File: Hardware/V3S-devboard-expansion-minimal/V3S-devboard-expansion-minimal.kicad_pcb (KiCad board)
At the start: 2 copper layers, 67.3 x 87.1 mm, 48 parts, among them CN1 AS0BC21-S30BE-7H, J1 Conn_01x05_Pin, J10 USB_C_Receptacle_USB2.0, J11 Conn_01x02_Pin, J12 Conn_02x05_Odd_Even, J13 Conn_01x03_Pin, J16 Conn_01x04_MountingPin, J17 Conn_01x04_MountingPin, J2 Conn_01x05_Pin, J3 Conn_01x05_Pin, J4 Conn_01x02_Pin, J5 Conn_02x05_Odd_Even, J6 Conn_01x02_Pin, J7 Conn_02x12_Odd_Even, J8 RJ45_Hanrun_HR911105A_Horizon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, U1 CP2102N-Axx-xQFN28, U3 AMS1117-3.3, U4 AMS1117-2.85

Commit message: working on final touches
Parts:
- added H1: MountingHole_Pad, v3s-devboard-expansion-minimal:screwnut, F.Cu at (98.5, 82.3)
- added R15: 8.2K, Resistor_SMD:R_0603_1608Metric, F.Cu at (81.0, 75.6)
- added R16: 10K, Resistor_SMD:R_0603_1608Metric, F.Cu at (81.0, 80.3)
- added R17: 11K, Resistor_SMD:R_0603_1608Metric, F.Cu at (81.0, 85.0)
- added R18: 6.8K, Resistor_SMD:R_0603_1608Metric, F.Cu at (81.7, 72.1)
- added SW1: SW_MEC_5E, v3s-devboard-module:SW_SKRPACE010, F.Cu at (75.6, 152.4)
- added SW2: SW_MEC_5E, v3s-devboard-module:SW_SKRPACE010, F.Cu at (77.0, 73.1)
- added SW3: SW_MEC_5E, v3s-devboard-module:SW_SKRPACE010, F.Cu at (77.0, 77.8)
- added SW4: SW_MEC_5E, v3s-devboard-module:SW_SKRPACE010, F.Cu at (77.0, 82.6)
- added SW5: SW_MEC_5E, v3s-devboard-module:SW_SKRPACE010, F.Cu at (77.0, 87.3)
- C5, C6: moved to B.Cu
- J16, J17: moved to F.Cu
- moved R6 114.0 mm to (74.8, 148.6)
- moved C6 23.6 mm to (134.7, 144.1)
- moved C5 21.9 mm to (134.7, 142.5)
- moved J17 21.8 mm to (134.1, 123.7), turned to 90 degrees
- moved JP8 19.7 mm to (125.6, 125.3)
- moved JP6 19.7 mm to (128.5, 122.2)
- moved J10 12.1 mm to (131.1, 153.0), turned to 0 degrees
- moved JP5 11.2 mm to (129.2, 108.9)
- moved JP7 11.2 mm to (126.3, 111.5)
- moved R14 10.0 mm to (133.7, 146.5), turned to 0 degrees
- moved J12 9.94 mm to (121.5, 116.4), turned to 0 degrees
- moved J16 9.57 mm to (134.1, 108.0), turned to 90 degrees
- moved R13 8.38 mm to (136.8, 138.5)
- moved U1 8.38 mm to (131.7, 138.3)
- moved C3 7.47 mm to (136.8, 141.7)
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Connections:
- J13 pad 2: LED_VDD -> LCD_VDD
- J3 pad 1: LED_VDD -> LCD_VDD
- J3 pad 2: LED_VDD -> LCD_VDD
- J3 pad 3: LED_VDD -> LCD_VDD
- J3 pad 4: LED_VDD -> LCD_VDD
- J3 pad 5: LED_VDD -> LCD_VDD
- J4 pad 1: LED_VDD -> LCD_VDD
- J7 pad 19: 3V3 -> GND
- J7 pad 20: GND -> 3V3
- J7 pad 21: 3V3 -> GND
- J7 pad 22: GND -> 3V3
- J7 pad 23: 3V3 -> GND
- J7 pad 24: GND -> 3V3
- R6 pad 1: LED_VDD -> LCD_VDD
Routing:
- net 3V3: track 99.0 -> 179.3 mm, vias 1 -> 5
- net /LRADC0: track 0.00 -> 73.8 mm, vias 0 -> 4
- net LCD_VDD: track 0.00 -> 73.4 mm, vias 0 -> 1
- net /SDC1.CLK: track 0.00 -> 63.6 mm, vias 0 -> 4
- net /SDC1.D0: track 0.00 -> 59.2 mm, vias 0 -> 4
- net /RESET: track 0.00 -> 51.3 mm, vias 0 -> 2
- net /USB.USB_ID: track 0.00 -> 44.5 mm, vias 0 -> 2
- net /LEDA: track 0.00 -> 36.4 mm
- net /CSI.MCSI_D0_N: track 24.2 -> 47.6 mm, vias 1 -> 2
- net /CSI.MCSI_D1_P: track 23.8 -> 46.2 mm, vias 1 -> 2
- net /CSI.MCSI_D1_N: track 23.2 -> 42.9 mm, vias 1 -> 2
- net /UART0.RX: track 40.1 -> 59.5 mm
- net /VBUS_IN: track 66.6 -> 86.0 mm
- net Net-(J12-Pin_1): track 28.5 -> 45.6 mm
- net /UART2.RX: track 57.9 -> 45.4 mm, vias 2 -> 3
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- added copper zone on B.Cu, net GND
- added copper zone on F.Cu, net GND
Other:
- board size 67.3 x 87.1 mm -> 68.5 x 88 mm

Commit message: Minor changes. Sent to fab
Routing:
- net /LCD_TE: track 48.4 -> 51.2 mm
- net /CSI.CSI_SDA: track 32.0 -> 34.7 mm
- net /UART0.TX: vias 6 -> 5
- net /UART0.RX: vias 4 -> 3
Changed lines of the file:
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@@
 		(sheetname "Root")
 		(sheetfile "V3S-devboard-expansion-minimal.kicad_sch")
-		(attr through_hole)
+		(attr through_hole exclude_from_bom)
 		(fp_line
 			(start 1.33 -1.33)
@@
 		(sheetname "Root")
 		(sheetfile "V3S-devboard-expansion-minimal.kicad_sch")
-		(attr smd)
+		(attr smd exclude_from_bom)
 		(fp_line
 			(start -4.04 -5.84)
@@
 			)
 		)
-		(property "LCSC" "C60491"
+		(property "LCSC" "C23212"
 			(at 0 0 180)
 			(unlocked yes)
@@
 		(sheetname "Root")
 		(sheetfile "V3S-devboard-expansion-minimal.kicad_sch")
-		(attr smd)
+		(attr smd exclude_from_bom)
 		(fp_line
 			(start -0.237258 0.5225)
@@
 		(sheetname "Root")
 		(sheetfile "V3S-devboard-expansion-minimal.kicad_sch")
-		(attr through_hole)
+		(attr through_hole exclude_from_bom)
 		(fp_line
 			(start -1.33 -1.33)
@@
 		(sheetname "Root")
 		(sheetfile "V3S-devboard-expansion-minimal.kicad_sch")
-		(attr smd)
+		(attr smd exclude_from_bom)
 		(fp_line
 			(start -0.237258 0.5225)
@@
 		(sheetname "Root")
 		(sheetfile "V3S-devboard-expansion-minimal.kicad_sch")
-		(attr through_hole)
+		(attr through_hole exclude_from_bom)
 		(fp_line
 			(start -1.33 -1.33)
@@
 			)
 		)
+		(property "LCSC" "C2928188"
+			(at 0 0 0)
+			(unlocked yes)
+			(layer "F.Fab")
+			(hide yes)
+			(effects
+				(font
+					(size 1 1)
+					(thickness 0.15)
+				)
+			)
+		)
 		(property ki_fp_filters "MountingHole*Pad*")
 		(sheetname "Root")
@@
 		(sheetname "Root")
 		(sheetfile "V3S-devboard-expansion-minimal.kicad_sch")
-		(attr through_hole)
+		(attr through_hole exclude_from_bom)
 		(fp_line
 			(start 3.87 -1.33)
@@
 		(sheetname "Root")
 		(sheetfile "V3S-devboard-expansion-minimal.kicad_sch")
-		(attr smd)
+		(attr smd exclude_from_bom)
 		(fp_line
 			(start -0.237258 0.5225)
@@
 		(sheetname "Root")
 		(sheetfile "V3S-devboard-expansion-minimal.kicad_sch")
-		(attr through_hole)
+		(attr through_hole exclude_from_bom)
 		(fp_line
 			(start -1.33 3.87)
@@
 			)
 		)
-		(property "LCSC" "C60491"
+		(property "LCSC" "C103227"
 			(at 0 0 -90)
 			(unlocked yes)
@@
 			)
 		)
+		(property "LCSC" "C139797"
+			(at 0 0 180)
+			(unlocked yes)
+			(layer "F.Fab")
+			(hide yes)
+			(effects
+				(font
+					(size 1 1)
+					(thickness 0.15)
+				)
+			)
+		)
 		(property ki_fp_filters "SW*MEC*5G*")
 		(sheetname "Root")
@@
 			)
 		)
+		(property "LCSC" "C139797"
+			(at 0 0 90)
+			(unlocked yes)
+			(layer "F.Fab")
+			(hide yes)
+			(effects
+				(font
+					(size 1 1)
+					(thickness 0.15)
+				)
+			)
+		)
 		(property ki_fp_filters "SW*MEC*5G*")
 		(sheetname "Root")
@@
 			)
 		)
+		(property "LCSC" "C2685134"
+			(at 0 0 180)
+			(unlocked yes)
+			(layer "F.Fab")
+			(hide yes)
+			(effects
+				(font
+					(size 1 1)
+					(thickness 0.15)
+				)
+			)
+		)
 		(property ki_fp_filters "Connector*:*_2x??_*")
 		(sheetname "Root")
@@
 			)
 		)
-		(property "LCSC" "C60491"
+		(property "LCSC" "C25804"
 			(at 0 0 -90)
 			(unlocked yes)
@@
 		(sheetname "Root")
 		(sheetfile "V3S-devboard-expansion-minimal.kicad_sch")
-		(attr smd)
+		(attr smd exclude_from_bom)
 		(fp_line
 			(start -0.237258 0.5225)
@@
 			)
 		)
+		(property "LCSC" "C2894897"
+			(at 0 0 0)
+			(unlocked yes)
+			(layer "F.Fab")
+			(hide yes)
+			(effects
+				(font
+					(size 1 1)
+					(thickness 0.15)
+				)
+			)
+		)
 		(property ki_fp_filters "USB*C*Receptacle*")
 		(sheetname "Root")
@@
 			)
 		)
-		(property "LCSC" "C60491"
+		(property "LCSC" "C25981"
 			(at 0 0 -90)
 			(unlocked yes)
@@
 		(sheetname "Root")
 		(sheetfile "V3S-devboard-expansion-minimal.kicad_sch")
-		(attr through_hole)
+		(attr through_hole exclude_from_bom)
 		(fp_line
 			(start -1.33 -1.33)
@@
 			)
 		)
+		(property "LCSC" "C139797"
+			(at 0 0 180)
+			(unlocked yes)
+			(layer "F.Fab")
+			(hide yes)
+			(effects
+				(font
+					(size 1 1)
+					(thickness 0.15)
+				)
+			)
+		)
 		(property ki_fp_filters "SW*MEC*5G*")
 		(sheetname "Root")
@@
 		(sheetname "Root")
 		(sheetfile "V3S-devboard-expansion-minimal.kicad_sch")
-		(attr through_hole)
+		(attr through_hole exclude_from_bom)
 		(fp_line
 			(start -1.33 -1.33)
@@
 		(sheetname "Root")
 		(sheetfile "V3S-devboard-expansion-minimal.kicad_sch")
-		(attr through_hole)
+		(attr through_hole exclude_from_bom)
 		(fp_line
 			(start -1.33 -1.33)
@@
 			)
 		)
+		(property "LCSC" "C139797"
+			(at 0 0 180)
+			(unlocked yes)
+			(layer "F.Fab")
+			(hide yes)
+			(effects
+				(font
+					(size 1 1)
+					(thickness 0.15)
+				)
+			)
+		)
 		(property ki_fp_filters "SW*MEC*5G*")
 		(sheetname "Root")
@@
 		(sheetname "Root")
 		(sheetfile "V3S-devboard-expansion-minimal.kicad_sch")
-		(attr smd)
+		(attr smd exclude_from_bom)
 		(fp_line
 			(start -0.153641 -0.38)
@@
 			)
 		)
+		(property "LCSC" "C139797"
+			(at 0 0 180)
+			(unlocked yes)
+			(layer "F.Fab")
+			(hide yes)
+			(effects
+				(font
+					(size 1 1)
+					(thickness 0.15)
+				)
+			)
+		)
 		(property ki_fp_filters "SW*MEC*5G*")
 		(sheetname "Root")
@@
 		(sheetname "Root")
 		(sheetfile "V3S-devboard-expansion-minimal.kicad_sch")
-		(attr smd)
+		(attr smd exclude_from_bom)
 		(fp_line
 			(start 0.140581 0.51)
@@
 		(sheetname "Root")
 		(sheetfile "V3S-devboard-expansion-minimal.kicad_sch")
-		(attr smd)
+		(attr smd exclude_from_bom)
 		(fp_line
 			(start 0.140581 0.51)
@@
 		(net 5)
 	)
-	(via
-		(at 129.24 107.555001)
-		(size 0.25)
-		(drill 0.15)
-		(layers "F.Cu" "B.Cu")
-		(net 5)
-	)
 	(segment
 		(start 107.215 136.355)
@@
 		(net 37)
 	)
-	(via
-		(at 129.34 110.155001)
-		(size 0.25)
-		(drill 0.15)
-		(layers "F.Cu" "B.Cu")
-		(net 37)
-	)
 	(segment
 		(start 114.93 127.27)
@@
 	)
 	(segment
+		(start 86.84 117.5)
+		(end 86.84 117.47)
+		(width 0.127)
+		(layer "F.Cu")
+		(net 55)
+	)
+	(segment
+		(start 86.84 117.47)
+		(end 80.885 111.515)
+		(width 0.127)
+		(layer "F.Cu")
+		(net 55)
+	)
+	(segment
 		(start 88.59 123.61)
 		(end 96.04 131.06)
@@
 	)
 	(segment
-		(start 87.59 122.54)
-		(end 87.59 122.59)
-		(width 0.127)
-		(layer "F.Cu")
-		(net 55)
-	)
-	(segment
-		(start 96.04 131.06)
-		(end 96.04 137.244999)
+		(start 80.885 111.515)
+		(end 78.15 111.515)
 		(width 0.127)
 		(layer "F.Cu")
@@
 	)
 	(segment
-		(start 86.84 117.47)
-		(end 80.885 111.515)
+		(start 87.59 122.54)
+		(end 87.59 122.59)
 		(width 0.127)
 		(layer "F.Cu")
@@
 	)
 	(segment
-		(start 86.84 117.5)
-		(end 86.84 117.47)
+		(start 96.04 131.06)
+		(end 96.04 137.244999)
 		(width 0.127)
 		(layer "F.Cu")
@@
 	)
 	(segment
-		(start 76.35 122.97)
-		(end 75.78 123.54)
+		(start 75.61 126.755)
+		(end 76.86 125.505)
 		(width 0.127)
 		(layer "F.Cu")
@@
 	)
 	(segment
+		(start 80.96 122.97)
+		(end 77.15 122.97)
+		(width 0.127)
+		(layer "F.Cu")
+		(net 77)
+	)
+	(segment
+		(start 76.86 123.26)
+		(end 77.15 122.97)
+		(width 0.127)
+		(layer "F.Cu")
+		(net 77)
+	)
+	(segment
 		(start 104.56 149.17)
 		(end 104.55 149.16)
@@
 	)
 	(segment
-		(start 80.96 122.97)
-		(end 76.35 122.97)
+		(start 76.86 125.505)
+		(end 76.86 123.26)
 		(width 0.127)
 		(layer "F.Cu")

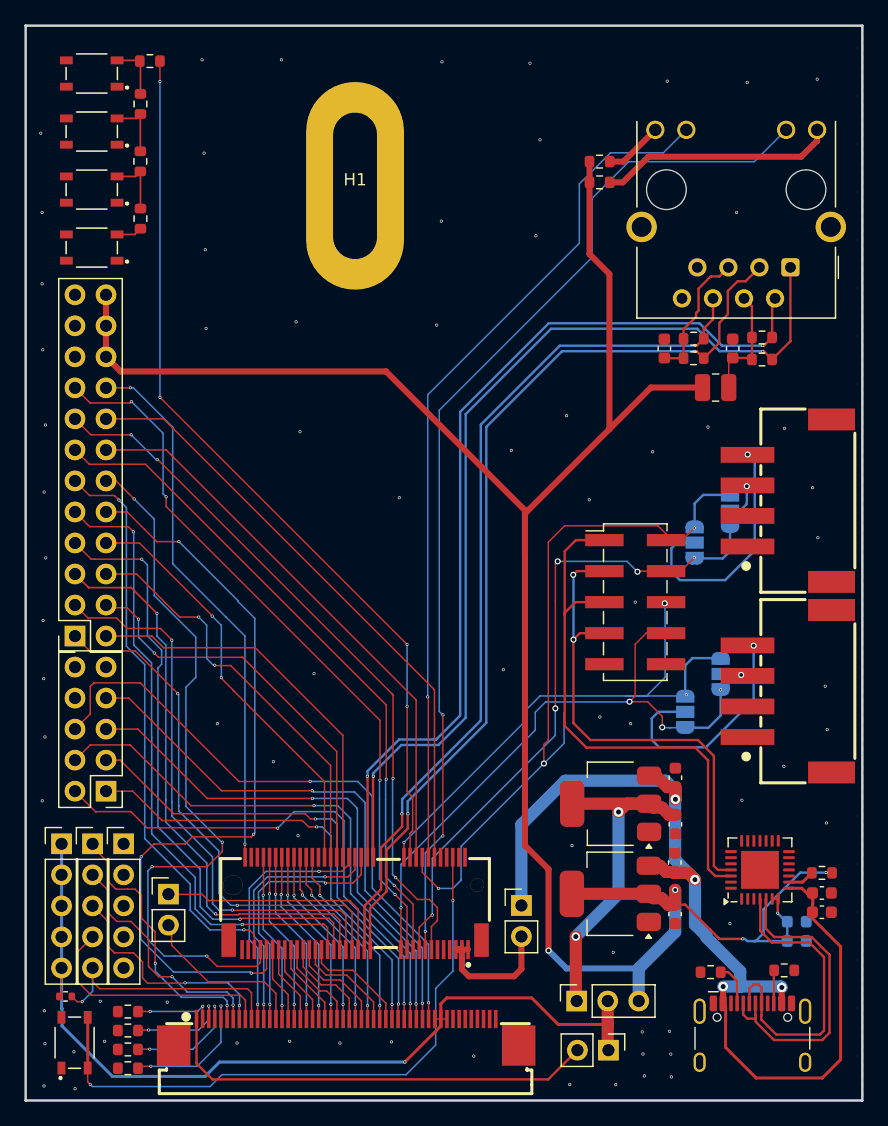
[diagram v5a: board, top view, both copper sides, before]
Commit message: fixed clearance problems, sent to fab
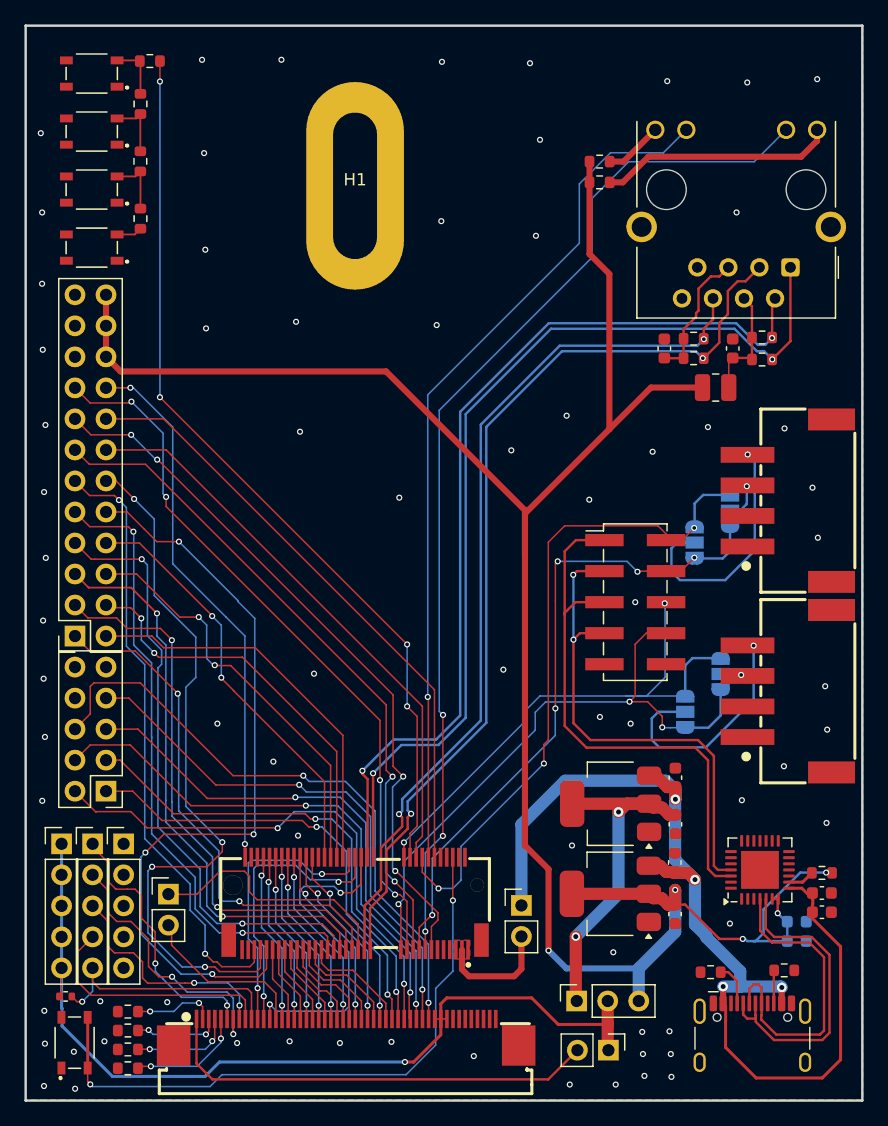
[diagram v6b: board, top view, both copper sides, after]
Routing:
- net /LCD0.CLK: track 21.3 -> 27.1 mm
- net /UART0.RX: track 59.5 -> 54.7 mm
- net /LCD0.VSYNC: track 20.5 -> 23.1 mm
- net /LCD0.HSYNC: track 20.9 -> 23.4 mm
- net /IM1: track 19.8 -> 22.3 mm
- net /SDC1.D2: track 47.6 -> 50.0 mm
- net /LEDK4: track 11.7 -> 9.59 mm
- net /LCD0.DE: track 19.4 -> 21.0 mm
- net /LEDK3: track 9.83 -> 8.33 mm
- net /LEDK2: track 8.35 -> 7.08 mm
- net 5V: track 10.7 -> 9.63 mm
- net /CSI.MCSI_D0_N: track 47.6 -> 46.9 mm
- net /CSI.MCSI_D0_P: track 50.5 -> 49.8 mm
- net /CSI.MCSI_D1_P: track 46.2 -> 45.5 mm
- net /CSI.MCSI_D1_N: track 42.9 -> 42.2 mm
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- added copper zone on F.Cu, net 5V
